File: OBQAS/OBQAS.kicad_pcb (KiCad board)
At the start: 2 copper layers, 150 x 100 mm, 146 parts, among them J1 24V IN, J2 USB_C_Receptacle_USB2.0, J3 K type, J5 TF_PUSH, J6 CH1, J7 CH2, K1 G5NB-1A-E_DC5, K2 G5NB-1A-E_DC5, K3 G5NB-1A-E_DC5, K4 G5NB-1A-E_DC5, Q1 IRLML2803TRPBF, Q2 IRLML2803TRPBF, Q3 IRLML2803TRPBF, Q4 IRLML2803TRPBF, Q5 BC846, Q6 BC846, Q7 IRLZ44N, Q8 IRLZ44N, Q9 IRFP064, SW1 SW_SPST, SW2 Enc, U1 LM7805_TO220, U2 AMS1117-3.3, U3 ESP32-WROOM-32, U4 CH340C, U5 TPS55288QWRPMRQ1, U6 LM358, U7 LM358, U8 MCP4921, U9 ADS1115IDGS

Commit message: inital routing complete
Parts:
- removed D1: LED, LED_SMD:LED_1206_3216Metric_Pad1.42x1.75mm_HandSolder
- removed R9: 470, Resistor_SMD:R_0805_2012Metric_Pad1.20x1.40mm_HandSolder
- removed REF** (x4): MountingHole_3.2mm_M3, MountingHole:MountingHole_3.2mm_M3
- added C22: 100n, Capacitor_SMD:C_0805_2012Metric_Pad1.18x1.45mm_HandSolder, F.Cu at (175.0, 80.2)
- added H1: MountingHole, MountingHole:MountingHole_3.2mm_M3, F.Cu at (72.9, 45.8)
- added H2: MountingHole, MountingHole:MountingHole_3.2mm_M3, F.Cu at (72.9, 138.8)
- added H3: MountingHole, MountingHole:MountingHole_3.2mm_M3, F.Cu at (145.0, 138.8)
- added H4: MountingHole, MountingHole:MountingHole_3.2mm_M3, F.Cu at (216.0, 45.8)
- Q9: moved to B.Cu
- R5, R6: value 10k -> 470
- TP15: footprint TestPoint:TestPoint_Pad_D2.5mm -> TestPoint:TestPoint_Pad_D1.0mm
- moved R25 166.8 mm to (172.0, 69.2), turned to 180 degrees
- moved R8 160.4 mm to (180.4, 47.7), turned to -90 degrees
- moved U8 157.0 mm to (175.2, 84.0)
- moved Q6 149.4 mm to (114.4, 103.6)
- moved R57 148.9 mm to (182.9, 98.3), turned to 90 degrees
- moved R61 148.0 mm to (202.4, 47.6)
- moved U6 147.8 mm to (175.2, 92.6), turned to 180 degrees
- moved D2 144.0 mm to (164.7, 134.9), turned to -90 degrees
- moved U9 142.9 mm to (174.2, 112.3)
- moved R54 140.9 mm to (181.9, 95.4)
- moved SW2 138.9 mm to (199.9, 53.9)
- moved R14 132.2 mm to (163.2, 107.4), turned to 180 degrees
- moved R62 132.1 mm to (217.5, 54.9), turned to 90 degrees
- moved R53 123.3 mm to (178.3, 117.6), turned to -90 degrees
- moved D4 123.2 mm to (158.8, 110.8)
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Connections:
- net Net-(J2-PadA6) renamed /D+
- net Net-(J2-PadA7) renamed /D-
- D2 pad 1: CH1R1 -> +5V
- D2 pad 2: GND -> CH1R1
- D3 pad 1: CH1R2 -> +5V
- D3 pad 2: GND -> CH1R2
- D4 pad 1: CH2R1 -> +5V
- D4 pad 2: GND -> CH2R1
- D5 pad 1: CH2R2 -> +5V
- D5 pad 2: GND -> CH2R2
- K1 pad 1: GND -> +5V
- K2 pad 4: GND -> +5V
- K3 pad 1: GND -> +5V
- K4 pad 4: GND -> +5V
- R25 pad 1: EN -> EN_UVLDO
- U3 pad 24: Net-(R9-Pad1) -> EN_UVLDO
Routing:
- net +5V: track 42.0 -> 462.5 mm, vias 3 -> 18
- net +3V3: track 111.7 -> 384.6 mm, vias 5 -> 12
- net SDA: track 1.23 -> 221.0 mm, vias 1 -> 7
- net SCL: track 2.52 -> 221.7 mm, vias 1 -> 2
- net ENC_B: track 0.00 -> 185.6 mm, vias 0 -> 7
- net ENC_Button: track 0.00 -> 179.4 mm, vias 0 -> 9
- net ENC_A: track 0.00 -> 169.1 mm, vias 0 -> 7
- net /D+: track 0.00 -> 144.0 mm, vias 0 -> 4
- net /D-: track 0.00 -> 143.6 mm, vias 0 -> 4
- net Net-(J3-Pad1): track 0.00 -> 143.2 mm, vias 0 -> 1
- net +2V5: track 0.00 -> 113.4 mm, vias 0 -> 4
- net EN_UVLDO: track 0.00 -> 111.1 mm, vias 0 -> 2
- net DAC_LDAC: track 0.00 -> 100.8 mm, vias 0 -> 2
- net HSPI_CLK: track 0.00 -> 100.2 mm, vias 0 -> 2
- net ADC_READY: track 0.00 -> 94.9 mm, vias 0 -> 5
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- added copper zone on B.Cu, net LOAD_IN
- added copper zone on F.Cu, net LOAD_IN
- added copper zone on B.Cu, net Net-(C11-Pad1)
- added copper zone on B.Cu, net Net-(F1-Pad1)
- added copper zone on B.Cu, net Net-(J1-Pad1)
- added copper zone on B.Cu, net Net-(K1-Pad2)
- added copper zone on B.Cu, net Net-(K3-Pad2)
- added copper zone on F.Cu, net Net-(K3-Pad2)
- added copper zone on B.Cu, net Net-(Q9-Pad3)
- added copper zone on F.Cu, net Net-(Q9-Pad3)
- added copper zone on B.Cu, net TPS_OUT
- added copper zone on F.Cu, net TPS_OUT
- added copper zone on B.Cu, net VCC

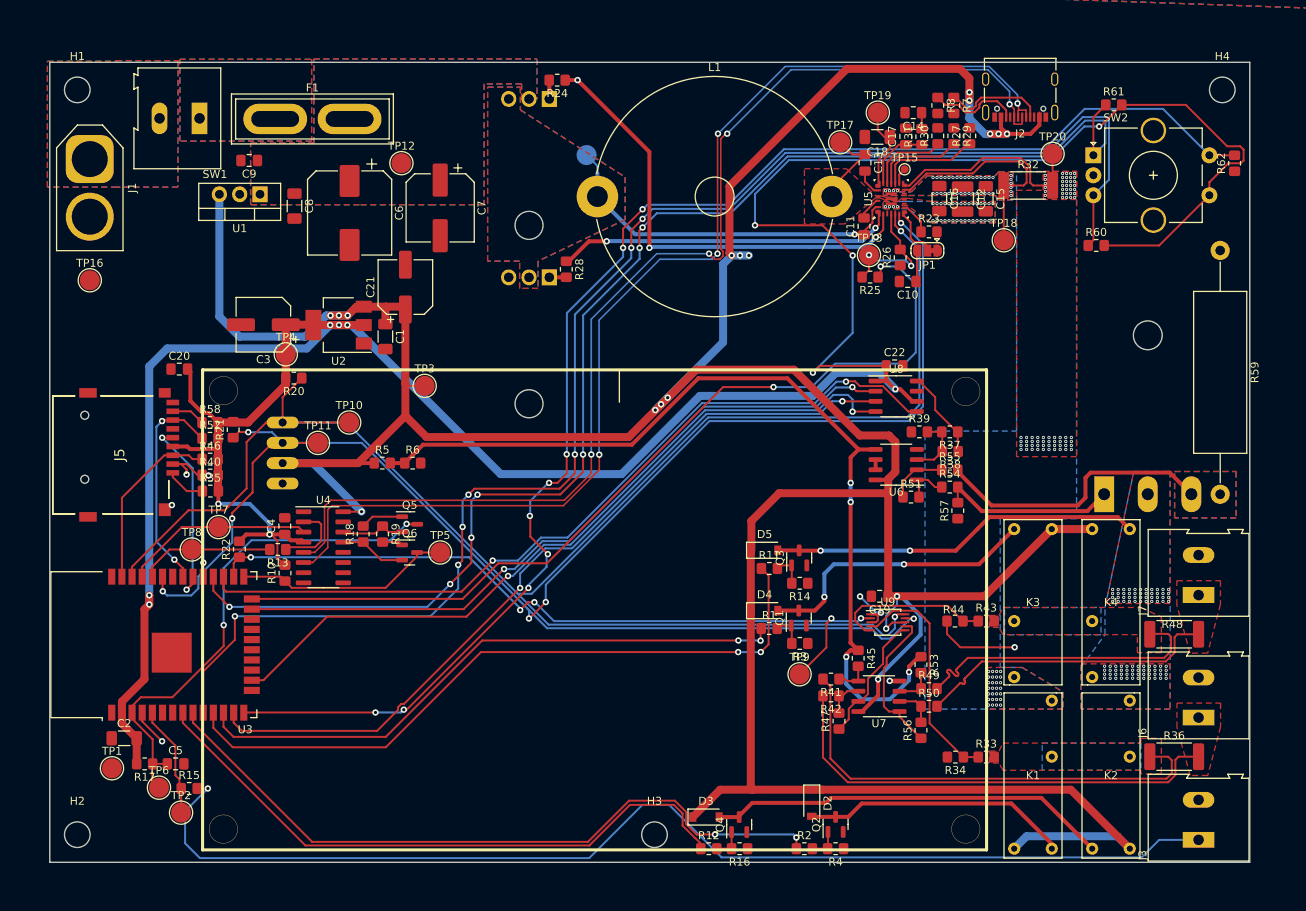
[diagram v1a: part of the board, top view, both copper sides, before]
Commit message: finished layout, doing silkscreen adjustment
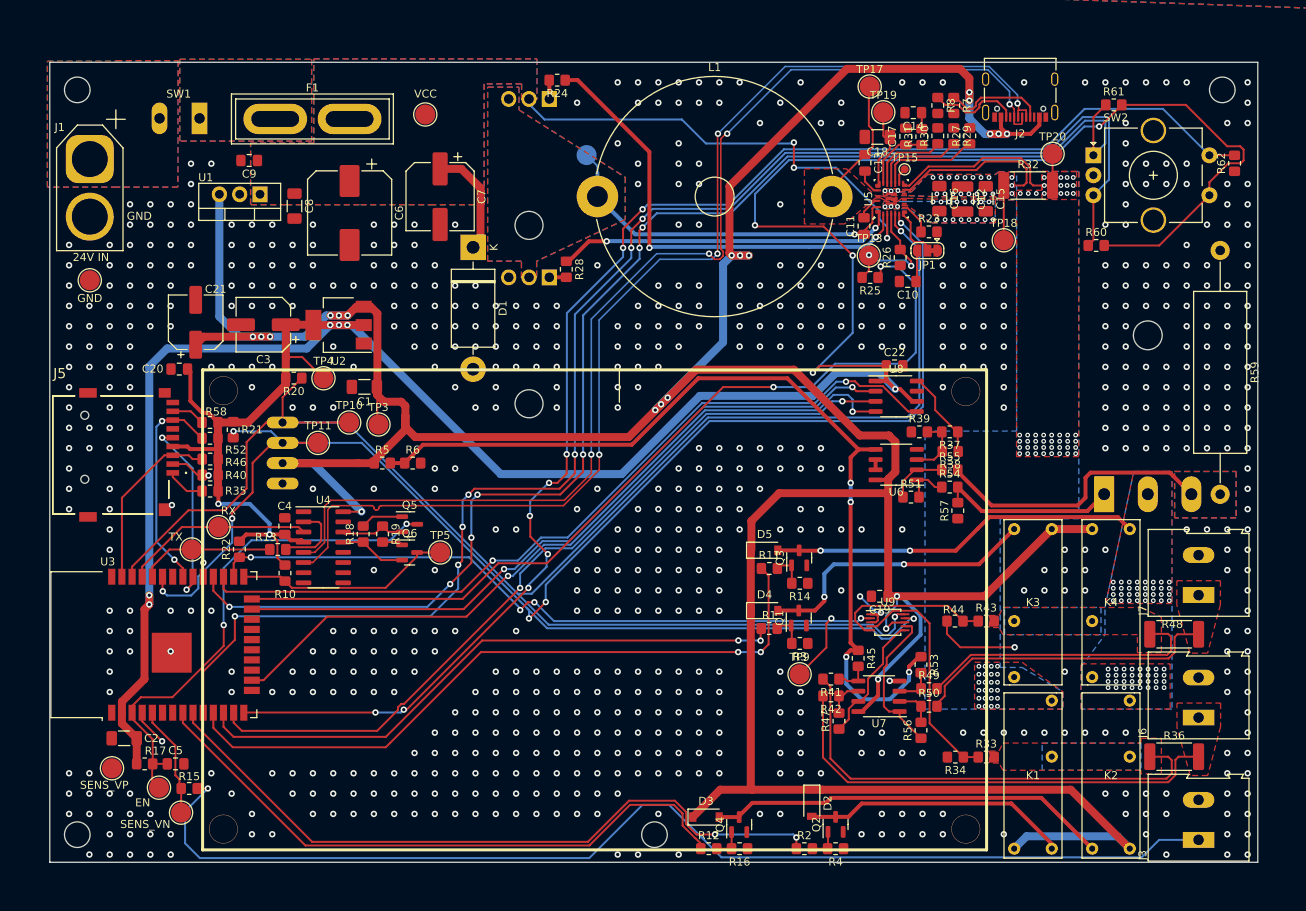
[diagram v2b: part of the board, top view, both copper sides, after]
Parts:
- added D1: 1N5408, Diode_THT:D_DO-201AD_P15.24mm_Horizontal, F.Cu at (122.3, 65.4)
- moved C21 26.6 mm to (87.7, 74.8)
- moved TP17 7.89 mm to (171.9, 45.3)
- moved TP3 7.53 mm to (110.5, 87.6)
- moved C1 6.81 mm to (108.8, 82.9), turned to 180 degrees
- moved TP12 6.78 mm to (116.4, 48.8)
- moved TP4 5.59 mm to (103.7, 81.8)
- moved C7 1.40 mm to (118.2, 59.1)
- moved TP19 0.69 mm to (173.6, 48.5)
- moved TP13 0.05 mm to (171.8, 66.5)
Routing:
- net VCC: track 0.00 -> 72.6 mm, vias 0 -> 3
- net +5V: track 462.5 -> 473.5 mm, vias 18 -> 21
- net +3V3: track 384.6 -> 390.3 mm
- net Net-(C13-Pad1): track 10.7 -> 16.1 mm
- net SD_SS: track 20.6 -> 18.0 mm, vias 3 -> 2
- net Net-(K3-Pad2): track 38.0 -> 35.8 mm
- net /D-: track 143.6 -> 144.2 mm
- net SDA: track 221.0 -> 221.5 mm
- net TPS_OUT: vias 102 -> 71
- net Net-(C12-Pad1): vias 42 -> 22
- net Net-(R24-Pad1): vias 3 -> 2
- net LOAD_IN: vias 92 -> 64
- net GND: vias 42 -> 790
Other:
- board size 150 x 100 mm -> 151 x 100 mm
- board text added: "GND"
